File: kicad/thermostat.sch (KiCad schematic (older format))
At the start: 10 parts, among them P1 Conn_02x20_Odd_Even, U1 PanasonicRelay

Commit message: screw terminals
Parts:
- added THERM_CONN: THERM_CONN, symbol Connector:Screw_Terminal_01x04
- U1: value PanasonicRelay -> RELAY_HEAT
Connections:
- net labels added: HVAC_AC(YELLOW), HVAC_FAN(GREEN), HVAC_HEAT(WHITE), HVAC_PWR(RED)
- wire segments 61 -> 65
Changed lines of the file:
@@
 EESchema Schematic File Version 4
 LIBS:thermostat-cache
-EELAYER 29 0
+EELAYER 30 0
 EELAYER END
 $Descr A4 11693 8268
@@
 	2100 4300 2500 4300
 $Comp
+L Connector:Screw_Terminal_01x04 THERM_CONN
+U 1 1 5D5B6FC9
+P 6300 1550
+F 0 "THERM_CONN" H 6380 1496 50  0000 L CNN
+F 1 "THERM_CONN" H 6380 1451 50  0001 L CNN
+F 2 "" H 6300 1550 50  0001 C CNN
+F 3 "~" H 6300 1550 50  0001 C CNN
+	1    6300 1550
+	1    0    0    -1
+$EndComp
+Text Label 5300 1450 0    50   ~ 0
+HVAC_PWR(RED)
+Text Label 5300 1550 0    50   ~ 0
+HVAC_HEAT(WHITE)
+Text Label 5300 1650 0    50   ~ 0
+HVAC_AC(YELLOW)
+Text Label 5300 1750 0    50   ~ 0
+HVAC_FAN(GREEN)
+Wire Wire Line
+	5300 1450 6100 1450
+Wire Wire Line
+	6100 1550 5300 1550
+Wire Wire Line
+	5300 1650 6100 1650
+Wire Wire Line
+	5300 1750 6100 1750
+$Comp
 L thermostat-rescue:PanasonicRelay U1
 U 1 1 5D5B9F71
-P 7800 1850
-F 0 "U1" H 7500 2050 50  0001 C CNN
-F 1 "PanasonicRelay" H 8228 1875 50  0000 L CNN
-F 2 "project_footprints:AGQ210A03" H 7500 2050 50  0001 C CNN
-F 3 "" H 7500 2050 50  0001 C CNN
-	1    7800 1850
-	1    0    0    -1
+P 4900 4300
+F 0 "U1" H 4600 4500 50  0001 C CNN
+F 1 "RELAY_HEAT" H 5328 4325 50  0000 L CNN
+F 2 "project_footprints:AGQ210A03" H 4600 4500 50  0001 C CNN
+F 3 "" H 4600 4500 50  0001 C CNN
+	1    4900 4300
+	0    -1   -1   0
 $EndComp
 $EndSCHEMATC

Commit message: updates
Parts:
- removed U1: RELAY_HEAT, project_footprints:AGQ210A03, symbol thermostat-rescue:PanasonicRelay
- added U1: RELAY_HEAT, project_footprints:AGQ210A03, symbol thermostat-rescue:Relay?
- MK1, MK2, MK3, MK4: value M2.5 -> Mounting_Hole-Mechanical; footprint MountingHole:MountingHole_2.7mm_M2.5 -> Mounting_Holes:MountingHole_2.5mm_Pad
- THERM_CONN1: renamed from THERM_CONN; footprint (none) -> TerminalBlocks_Phoenix:TerminalBlock_Phoenix_MPT-2.54mm_4pol
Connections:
- wire segments 65 -> 69
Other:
- note removed: "Mounting Holes"
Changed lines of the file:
@@
 ID_SD and ID_SC PINS:\nThese pins are reserved for HAT ID EEPROM.\n\nAt boot time this I2C interface will be\ninterrogated to look for an EEPROM\nthat identifes the attached board and\nallows automagic setup of the GPIOs\n(and optionally, Linux drivers).\n\nDO NOT USE these pins for anything other\nthan attaching an I2C ID EEPROM. Leave\nunconnected if ID EEPROM not required.
-$Comp
-L thermostat-rescue:Mounting_Hole-Mechanical MK1
-U 1 1 5834FB2E
-P 3000 7200
-F 0 "MK1" H 3100 7246 50  0000 L CNN
-F 1 "M2.5" H 3100 7155 50  0000 L CNN
-F 2 "MountingHole:MountingHole_2.7mm_M2.5" H 3000 7200 60  0001 C CNN
-F 3 "" H 3000 7200 60  0001 C CNN
-	1    3000 7200
-	1    0    0    -1
-$EndComp
-$Comp
-L thermostat-rescue:Mounting_Hole-Mechanical MK3
-U 1 1 5834FBEF
-P 3450 7200
-F 0 "MK3" H 3550 7246 50  0000 L CNN
-F 1 "M2.5" H 3550 7155 50  0000 L CNN
-F 2 "MountingHole:MountingHole_2.7mm_M2.5" H 3450 7200 60  0001 C CNN
-F 3 "" H 3450 7200 60  0001 C CNN
-	1    3450 7200
-	1    0    0    -1
-$EndComp
-$Comp
-L thermostat-rescue:Mounting_Hole-Mechanical MK2
-U 1 1 5834FC19
-P 3000 7400
-F 0 "MK2" H 3100 7446 50  0000 L CNN
-F 1 "M2.5" H 3100 7355 50  0000 L CNN
-F 2 "MountingHole:MountingHole_2.7mm_M2.5" H 3000 7400 60  0001 C CNN
-F 3 "" H 3000 7400 60  0001 C CNN
-	1    3000 7400
-	1    0    0    -1
-$EndComp
-$Comp
-L thermostat-rescue:Mounting_Hole-Mechanical MK4
-U 1 1 5834FC4F
-P 3450 7400
-F 0 "MK4" H 3550 7446 50  0000 L CNN
-F 1 "M2.5" H 3550 7355 50  0000 L CNN
-F 2 "MountingHole:MountingHole_2.7mm_M2.5" H 3450 7400 60  0001 C CNN
-F 3 "" H 3450 7400 60  0001 C CNN
-	1    3450 7400
-	1    0    0    -1
-$EndComp
-Text Notes 3000 7050 0    50   ~ 0
-Mounting Holes
 $Comp
 L Connector_Generic:Conn_02x20_Odd_Even P1
@@
 GPIO16
 Text Label 850  4750 0    50   ~ 0
-GPIO17(GEN0)
+GPIO20(SPI1_MOSI)
 Text Label 850  5200 0    50   ~ 0
 GPIO21(SPI1_SCK)
 Text Label 850  5650 0    50   ~ 0
-GPIO22(GEN3)
+GPIO12(PWM0)
 Wire Wire Line
 	1700 4300 850  4300
@@
 	2100 4300 2500 4300
 $Comp
-L Connector:Screw_Terminal_01x04 THERM_CONN
+L Connector:Screw_Terminal_01x04 THERM_CONN1
 U 1 1 5D5B6FC9
 P 6300 1550
-F 0 "THERM_CONN" H 6380 1496 50  0000 L CNN
+F 0 "THERM_CONN1" H 6380 1496 50  0000 L CNN
 F 1 "THERM_CONN" H 6380 1451 50  0001 L CNN
-F 2 "" H 6300 1550 50  0001 C CNN
+F 2 "TerminalBlocks_Phoenix:TerminalBlock_Phoenix_MPT-2.54mm_4pol" H 6300 1550 50  0001 C CNN
 F 3 "~" H 6300 1550 50  0001 C CNN
 	1    6300 1550
@@
 	5300 1750 6100 1750
 $Comp
-L thermostat-rescue:PanasonicRelay U1
-U 1 1 5D5B9F71
-P 4900 4300
-F 0 "U1" H 4600 4500 50  0001 C CNN
-F 1 "RELAY_HEAT" H 5328 4325 50  0000 L CNN
-F 2 "project_footprints:AGQ210A03" H 4600 4500 50  0001 C CNN
-F 3 "" H 4600 4500 50  0001 C CNN
-	1    4900 4300
-	0    -1   -1   0
-$EndComp
+L thermostat-rescue:Relay? U1
+U 1 1 5D5E9059
+P 5900 2600
+F 0 "U1" V 6050 2800 50  0001 C CNN
+F 1 "RELAY_HEAT" H 5900 2923 50  0000 C CNN
+F 2 "project_footprints:AGQ210A03" V 6050 2800 50  0001 C CNN
+F 3 "" V 6050 2800 50  0001 C CNN
+	1    5900 2600
+	1    0    0    -1
+$EndComp
+$Comp
+L thermostat-rescue:Mounting_Hole-Mechanical MK1
+U 1 1 5D5E9722
+P 2950 6550
+F 0 "MK1" H 3050 6596 50  0000 L CNN
+F 1 "Mounting_Hole-Mechanical" H 3050 6505 50  0000 L CNN
+F 2 "Mounting_Holes:MountingHole_2.5mm_Pad" H 2950 6550 50  0001 C CNN
+F 3 "" H 2950 6550 50  0001 C CNN
+	1    2950 6550
+	1    0    0    -1
+$EndComp
+$Comp
+L thermostat-rescue:Mounting_Hole-Mechanical MK2
+U 1 1 5D5F78A7
+P 2950 6800
+F 0 "MK2" H 3050 6846 50  0000 L CNN
+F 1 "Mounting_Hole-Mechanical" H 3050 6755 50  0000 L CNN
+F 2 "Mounting_Holes:MountingHole_2.5mm_Pad" H 2950 6800 50  0001 C CNN
+F 3 "" H 2950 6800 50  0001 C CNN
+	1    2950 6800
+	1    0    0    -1
+$EndComp
+$Comp
+L thermostat-rescue:Mounting_Hole-Mechanical MK3
+U 1 1 5D5F9275
+P 2950 7050
+F 0 "MK3" H 3050 7096 50  0000 L CNN
+F 1 "Mounting_Hole-Mechanical" H 3050 7005 50  0000 L CNN
+F 2 "Mounting_Holes:MountingHole_2.5mm_Pad" H 2950 7050 50  0001 C CNN
+F 3 "" H 2950 7050 50  0001 C CNN
+	1    2950 7050
+	1    0    0    -1
+$EndComp
+$Comp
+L thermostat-rescue:Mounting_Hole-Mechanical MK4
+U 1 1 5D5FAC9B
+P 2950 7300
+F 0 "MK4" H 3050 7346 50  0000 L CNN
+F 1 "Mounting_Hole-Mechanical" H 3050 7255 50  0000 L CNN
+F 2 "Mounting_Holes:MountingHole_2.5mm_Pad" H 2950 7300 50  0001 C CNN
+F 3 "" H 2950 7300 50  0001 C CNN
+	1    2950 7300
+	1    0    0    -1
+$EndComp
+Text Label 5550 2650 2    50   ~ 0
+HVAC_PWR(RED)
+Text Label 5550 2550 2    50   ~ 0
+HVAC_HEAT(WHITE)
+Text Label 5550 2400 2    50   ~ 0
+GPIO5
+Text Label 6250 2400 0    50   ~ 0
+GPIO6
+Wire Wire Line
+	6250 2400 6050 2400
+Wire Wire Line
+	5750 2400 5550 2400
+Wire Wire Line
+	5750 2550 5550 2550
+Wire Wire Line
+	5750 2650 5550 2650
 $EndSCHEMATC

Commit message: First take at the bigger board
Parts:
- added RELAY_COOL1: RELAY_COOL, project_footprints:AGQ210A03, symbol thermostat-rescue:Relay?-thermostat-rescue
- added RELAY_HEAT1: RELAY_HEAT, project_footprints:AGQ210A03, symbol thermostat-rescue:Relay?-thermostat-rescue
- MK1, MK2, MK3, MK4: symbol thermostat-rescue:Mounting_Hole-Mechanical -> thermostat-rescue:Mounting_Hole-Mechanical-thermostat-rescue
- RELAY_FAN1: renamed from U1; value RELAY_HEAT -> RELAY_FAN; symbol thermostat-rescue:Relay? -> thermostat-rescue:Relay?-thermostat-rescue
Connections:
- net labels added: HVAC_COOL(YELLOW)
- net labels removed: HVAC_AC(YELLOW)
- wire segments 69 -> 77
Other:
- moved on the sheet: THERM_CONN1
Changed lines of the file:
@@
 L Connector:Screw_Terminal_01x04 THERM_CONN1
 U 1 1 5D5B6FC9
-P 6300 1550
-F 0 "THERM_CONN1" H 6380 1496 50  0000 L CNN
-F 1 "THERM_CONN" H 6380 1451 50  0001 L CNN
-F 2 "TerminalBlocks_Phoenix:TerminalBlock_Phoenix_MPT-2.54mm_4pol" H 6300 1550 50  0001 C CNN
-F 3 "~" H 6300 1550 50  0001 C CNN
-	1    6300 1550
+P 9850 1150
+F 0 "THERM_CONN1" H 9930 1096 50  0000 L CNN
+F 1 "THERM_CONN" H 9930 1051 50  0001 L CNN
+F 2 "TerminalBlocks_Phoenix:TerminalBlock_Phoenix_MPT-2.54mm_4pol" H 9850 1150 50  0001 C CNN
+F 3 "~" H 9850 1150 50  0001 C CNN
+	1    9850 1150
 	1    0    0    -1
 $EndComp
-Text Label 5300 1450 0    50   ~ 0
+Text Label 8850 1050 0    50   ~ 0
 HVAC_PWR(RED)
-Text Label 5300 1550 0    50   ~ 0
+Text Label 8850 1150 0    50   ~ 0
 HVAC_HEAT(WHITE)
-Text Label 5300 1650 0    50   ~ 0
-HVAC_AC(YELLOW)
-Text Label 5300 1750 0    50   ~ 0
+Text Label 8850 1250 0    50   ~ 0
+HVAC_COOL(YELLOW)
+Text Label 8850 1350 0    50   ~ 0
 HVAC_FAN(GREEN)
 Wire Wire Line
-	5300 1450 6100 1450
+	8850 1050 9650 1050
 Wire Wire Line
-	6100 1550 5300 1550
+	9650 1150 8850 1150
 Wire Wire Line
-	5300 1650 6100 1650
+	8850 1250 9650 1250
 Wire Wire Line
-	5300 1750 6100 1750
+	8850 1350 9650 1350
 $Comp
-L thermostat-rescue:Relay? U1
+L thermostat-rescue:Relay?-thermostat-rescue RELAY_FAN1
 U 1 1 5D5E9059
-P 5900 2600
-F 0 "U1" V 6050 2800 50  0001 C CNN
-F 1 "RELAY_HEAT" H 5900 2923 50  0000 C CNN
-F 2 "project_footprints:AGQ210A03" V 6050 2800 50  0001 C CNN
-F 3 "" V 6050 2800 50  0001 C CNN
-	1    5900 2600
+P 6200 1250
+F 0 "RELAY_FAN1" V 6350 1450 50  0001 C CNN
+F 1 "RELAY_FAN" H 6200 1573 50  0000 C CNN
+F 2 "project_footprints:AGQ210A03" V 6350 1450 50  0001 C CNN
+F 3 "" V 6350 1450 50  0001 C CNN
+	1    6200 1250
 	1    0    0    -1
 $EndComp
 $Comp
-L thermostat-rescue:Mounting_Hole-Mechanical MK1
+L thermostat-rescue:Mounting_Hole-Mechanical-thermostat-rescue MK1
 U 1 1 5D5E9722
 P 2950 6550
@@
 $EndComp
 $Comp
-L thermostat-rescue:Mounting_Hole-Mechanical MK2
+L thermostat-rescue:Mounting_Hole-Mechanical-thermostat-rescue MK2
 U 1 1 5D5F78A7
 P 2950 6800
@@
 $EndComp
 $Comp
-L thermostat-rescue:Mounting_Hole-Mechanical MK3
+L thermostat-rescue:Mounting_Hole-Mechanical-thermostat-rescue MK3
 U 1 1 5D5F9275
 P 2950 7050
@@
 $EndComp
 $Comp
-L thermostat-rescue:Mounting_Hole-Mechanical MK4
+L thermostat-rescue:Mounting_Hole-Mechanical-thermostat-rescue MK4
 U 1 1 5D5FAC9B
 P 2950 7300
@@
 	1    0    0    -1
 $EndComp
-Text Label 5550 2650 2    50   ~ 0
+Text Label 6550 1050 0    50   ~ 0
+GPIO19(SPI1_MISO)
+Wire Wire Line
+	6550 1050 6350 1050
+Wire Wire Line
+	6050 1050 5850 1050
+Wire Wire Line
+	6050 1200 5850 1200
+Wire Wire Line
+	6050 1300 5850 1300
+Text Label 5850 1050 2    50   ~ 0
+GPIO5
+Text Label 5850 1200 2    50   ~ 0
+HVAC_FAN(GREEN)
+Text Label 5850 1300 2    50   ~ 0
 HVAC_PWR(RED)
-Text Label 5550 2550 2    50   ~ 0
+$Comp
+L thermostat-rescue:Relay?-thermostat-rescue RELAY_HEAT1
+U 1 1 5D5EC4AE
+P 6200 1950
+F 0 "RELAY_HEAT1" V 6350 2150 50  0001 C CNN
+F 1 "RELAY_HEAT" H 6200 2273 50  0000 C CNN
+F 2 "project_footprints:AGQ210A03" V 6350 2150 50  0001 C CNN
+F 3 "" V 6350 2150 50  0001 C CNN
+	1    6200 1950
+	1    0    0    -1
+$EndComp
+Text Label 6550 1750 0    50   ~ 0
+GPIO19(SPI1_MISO)
+Wire Wire Line
+	6550 1750 6350 1750
+Wire Wire Line
+	6050 1750 5850 1750
+Wire Wire Line
+	6050 1900 5850 1900
+Wire Wire Line
+	6050 2000 5850 2000
+Text Label 5850 1750 2    50   ~ 0
+GPIO6
+Text Label 5850 1900 2    50   ~ 0
 HVAC_HEAT(WHITE)
-Text Label 5550 2400 2    50   ~ 0
-GPIO5
-Text Label 6250 2400 0    50   ~ 0
-GPIO6
+Text Label 5850 2000 2    50   ~ 0
+HVAC_PWR(RED)
+$Comp
+L thermostat-rescue:Relay?-thermostat-rescue RELAY_COOL1
+U 1 1 5D5EE68E
+P 6200 2650
+F 0 "RELAY_COOL1" V 6350 2850 50  0001 C CNN
+F 1 "RELAY_COOL" H 6200 2973 50  0000 C CNN
+F 2 "project_footprints:AGQ210A03" V 6350 2850 50  0001 C CNN
+F 3 "" V 6350 2850 50  0001 C CNN
+	1    6200 2650
+	1    0    0    -1
+$EndComp
+Text Label 6550 2450 0    50   ~ 0
+GPIO19(SPI1_MISO)
 Wire Wire Line
-	6250 2400 6050 2400
+	6550 2450 6350 2450
 Wire Wire Line
-	5750 2400 5550 2400
+	6050 2450 5850 2450
 Wire Wire Line
-	5750 2550 5550 2550
+	6050 2600 5850 2600
 Wire Wire Line
-	5750 2650 5550 2650
+	6050 2700 5850 2700
+Text Label 5850 2450 2    50   ~ 0
+GPIO13(PWM1)
+Text Label 5850 2600 2    50   ~ 0
+HVAC_COOL(YELLOW)
+Text Label 5850 2700 2    50   ~ 0
+HVAC_PWR(RED)
 $EndSCHEMATC

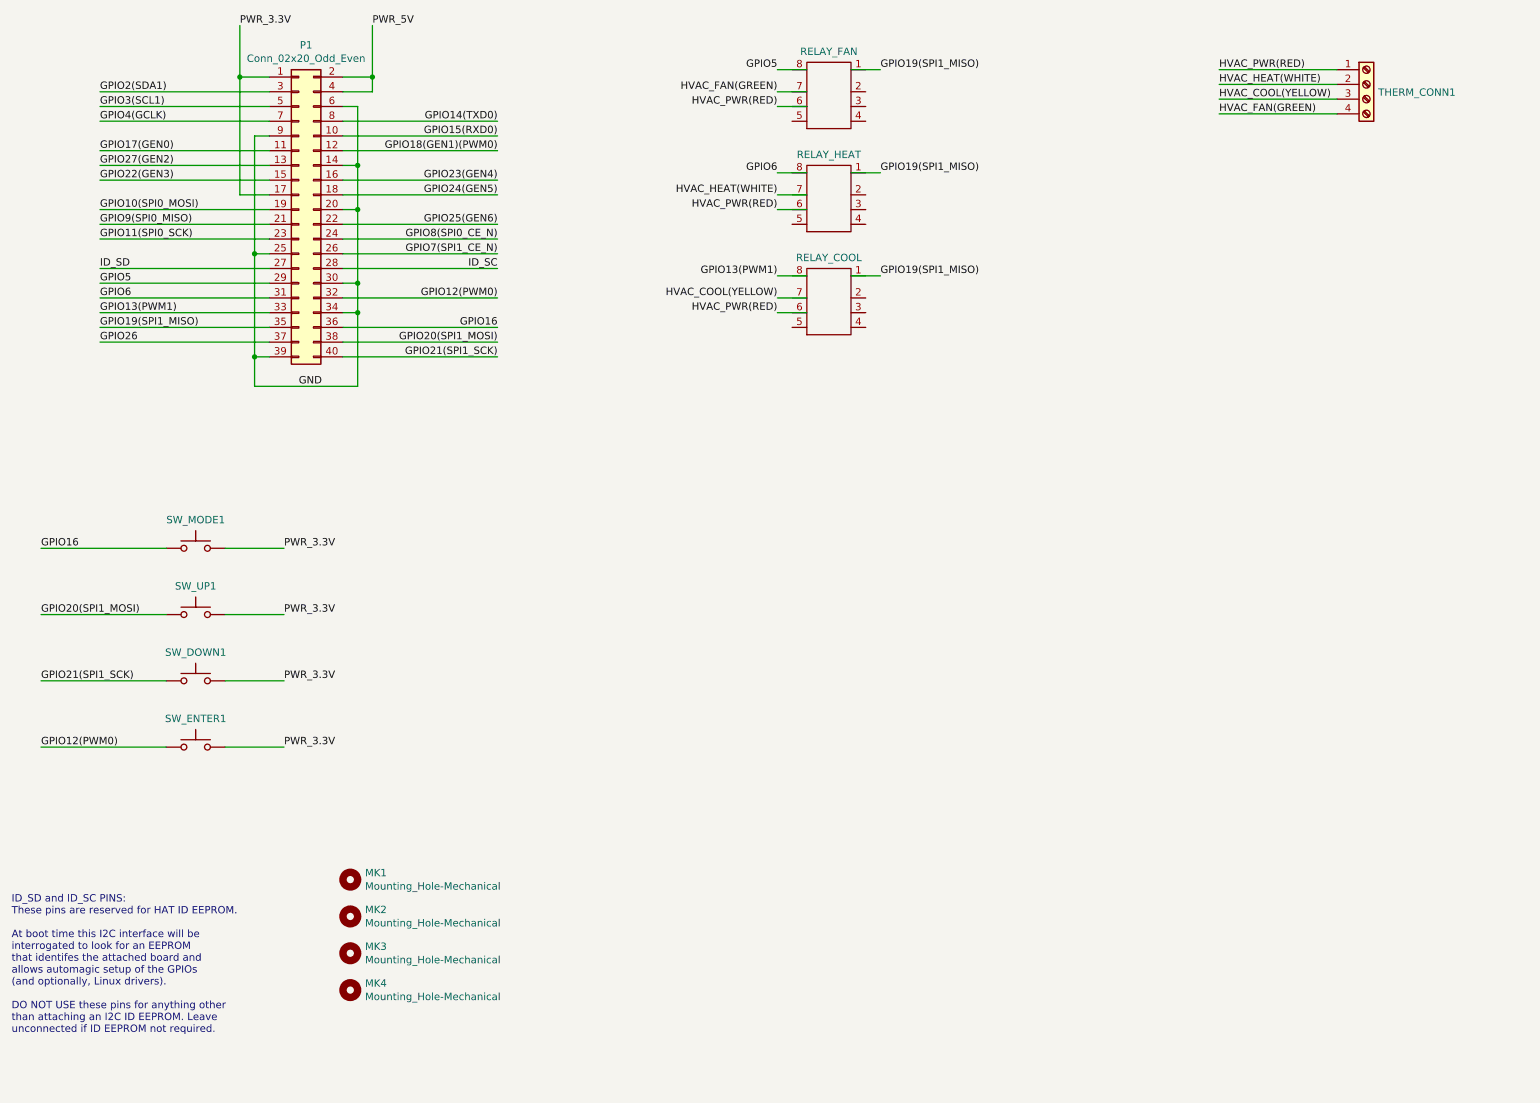
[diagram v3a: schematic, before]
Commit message: Almost ready for ethernet header
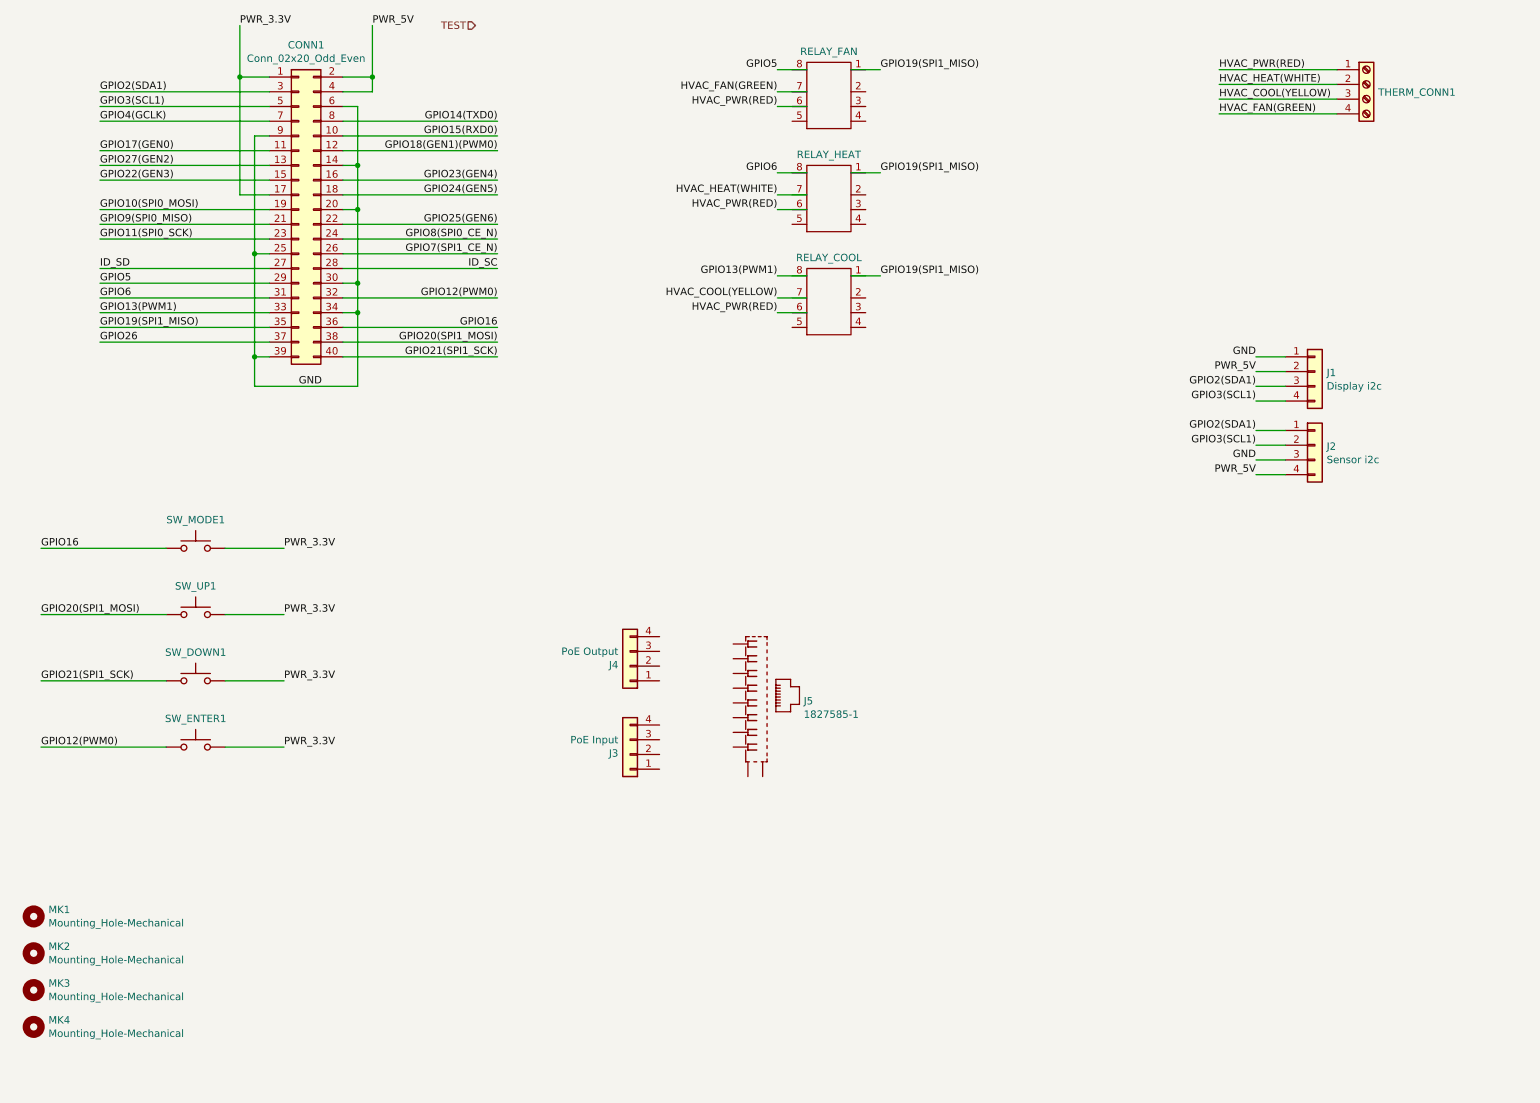
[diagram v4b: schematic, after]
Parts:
- added J1: Display i2c, Socket_Strips:Socket_Strip_Angled_1x04_Pitch2.54mm, symbol Connector_Generic:Conn_01x04
- added J2: Sensor i2c, Socket_Strips:Socket_Strip_Straight_1x04_Pitch2.54mm, symbol Connector_Generic:Conn_01x04
- added J3: PoE Input, Socket_Strips:Socket_Strip_Angled_1x04_Pitch2.54mm, symbol Connector_Generic:Conn_01x04
- added J4: PoE Output, Socket_Strips:Socket_Strip_Angled_1x04_Pitch2.54mm, symbol Connector_Generic:Conn_01x04
- added J5: 1827585-1, TE_1827585-1, symbol thermostat:1827585-1
- CONN1: renamed from P1; footprint Connector_PinSocket_2.54mm:PinSocket_2x20_P2.54mm_Vertical -> Socket_Strips:Socket_Strip_Straight_2x20_Pitch2.54mm
- RELAY1: renamed from RELAY_FAN1; MPN (none) -> AGQ210A03; Package (none) -> AGQ210A03; Populate (none) -> 1
- RELAY2: renamed from RELAY_HEAT1; MPN (none) -> AGQ210A03; Populate (none) -> 1
- RELAY3: renamed from RELAY_COOL1; MPN (none) -> AGQ210A03; Populate (none) -> 1
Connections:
- net GND: now also J1.1 (Pin_1), J2.3 (Pin_3)
- net GPIO2(SDA1): now also J1.3 (Pin_3), J2.1 (Pin_1)
- net GPIO3(SCL1): now also J1.4 (Pin_4), J2.2 (Pin_2)
- net PWR_5V: now also J1.2 (Pin_2), J2.4 (Pin_4)
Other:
- note removed: "ID_SD and ID_SC PINS:\nThese pins are reserved for HAT ID EEPROM.\n\nAt boot time this I2C interface will be\ninterrogated to look for an EEPROM\nthat identifes the attached board and\nallows automagic setup of the GPIOs\n(and optionally, Linux drivers).\n\nDO NOT USE these pins for anything other\nthan attaching an I2C ID EEPROM. Leave\nunconnected if ID EEPROM not required."
- moved on the sheet: MK1, MK2, MK3, MK4
